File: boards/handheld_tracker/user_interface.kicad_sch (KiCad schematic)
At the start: 0 parts

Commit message: added test pads, UI buttons, and routed MCU pins
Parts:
- added SW1, SW10, SW11, SW12, SW13, SW14, SW15, SW2, SW3, SW4, SW5, SW6, SW7, SW8, SW9: SW_Push, Button_Switch_SMD:SW_SPST_PTS645, symbol Switch:SW_Push
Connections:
- new net +3.3V: SW1.1, SW10.1, SW11.1, SW12.1, SW13.1, SW14.1, SW15.1, SW2.1, SW3.1, SW4.1, SW5.1, SW6.1, SW7.1, SW8.1, SW9.1
- new net pushbutton_0: SW11.2
- new net pushbutton_1: SW1.2
- new net pushbutton_2: SW4.2
- new net pushbutton_3: SW7.2
- new net pushbutton_4: SW2.2
- new net pushbutton_5: SW5.2
- new net pushbutton_6: SW8.2
- new net pushbutton_7: SW3.2
- new net pushbutton_8: SW6.2
- new net pushbutton_9: SW9.2
- new net pushbutton_dot: SW10.2
- new net pushbutton_down: SW15.2
- new net pushbutton_enter: SW12.2
- new net pushbutton_menu: SW13.2
- new net pushbutton_up: SW14.2
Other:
- note added: "."
- note added: "0"
- note added: "1"
- note added: "2"
- note added: "3"
- note added: "4"
- note added: "5"
- note added: "6"
- note added: "7"
- note added: "8"
- note added: "9"
- note added: "<"
- note added: ">"
- note added: "ENTER"
- note added: "MENU"

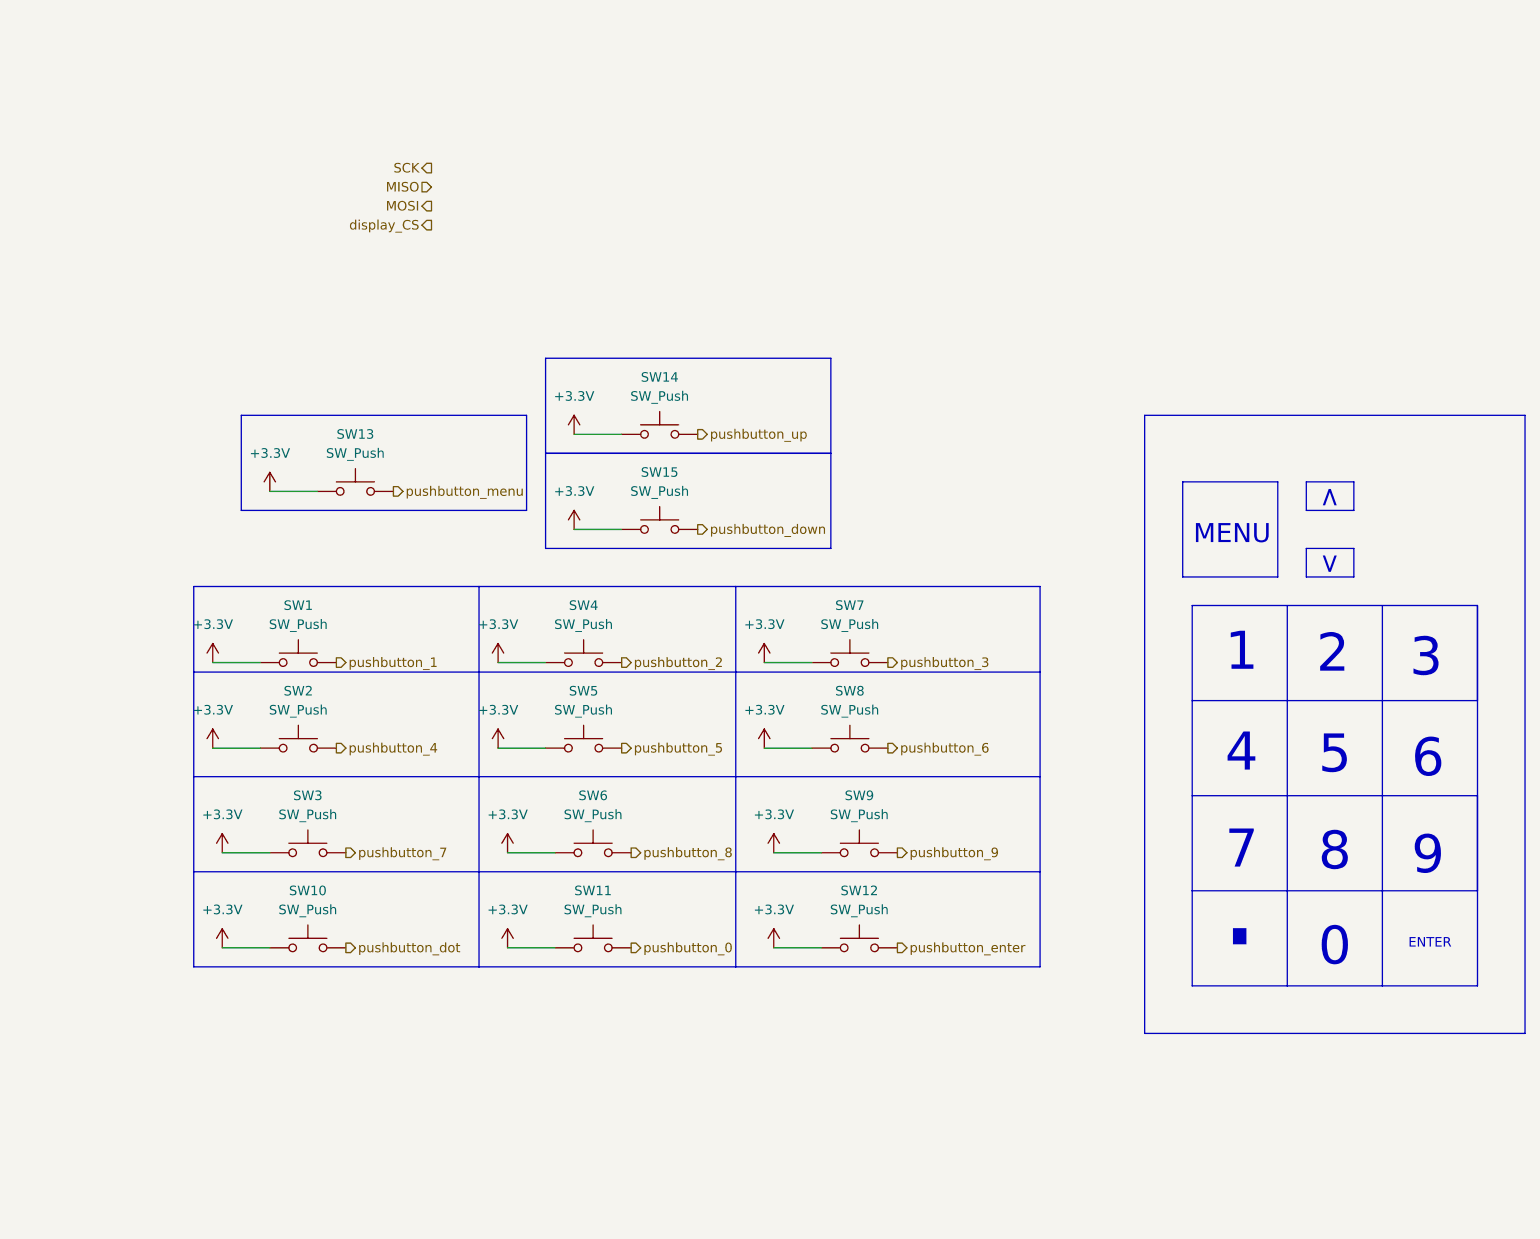
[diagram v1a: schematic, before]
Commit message: added all footprints and modified gitignore
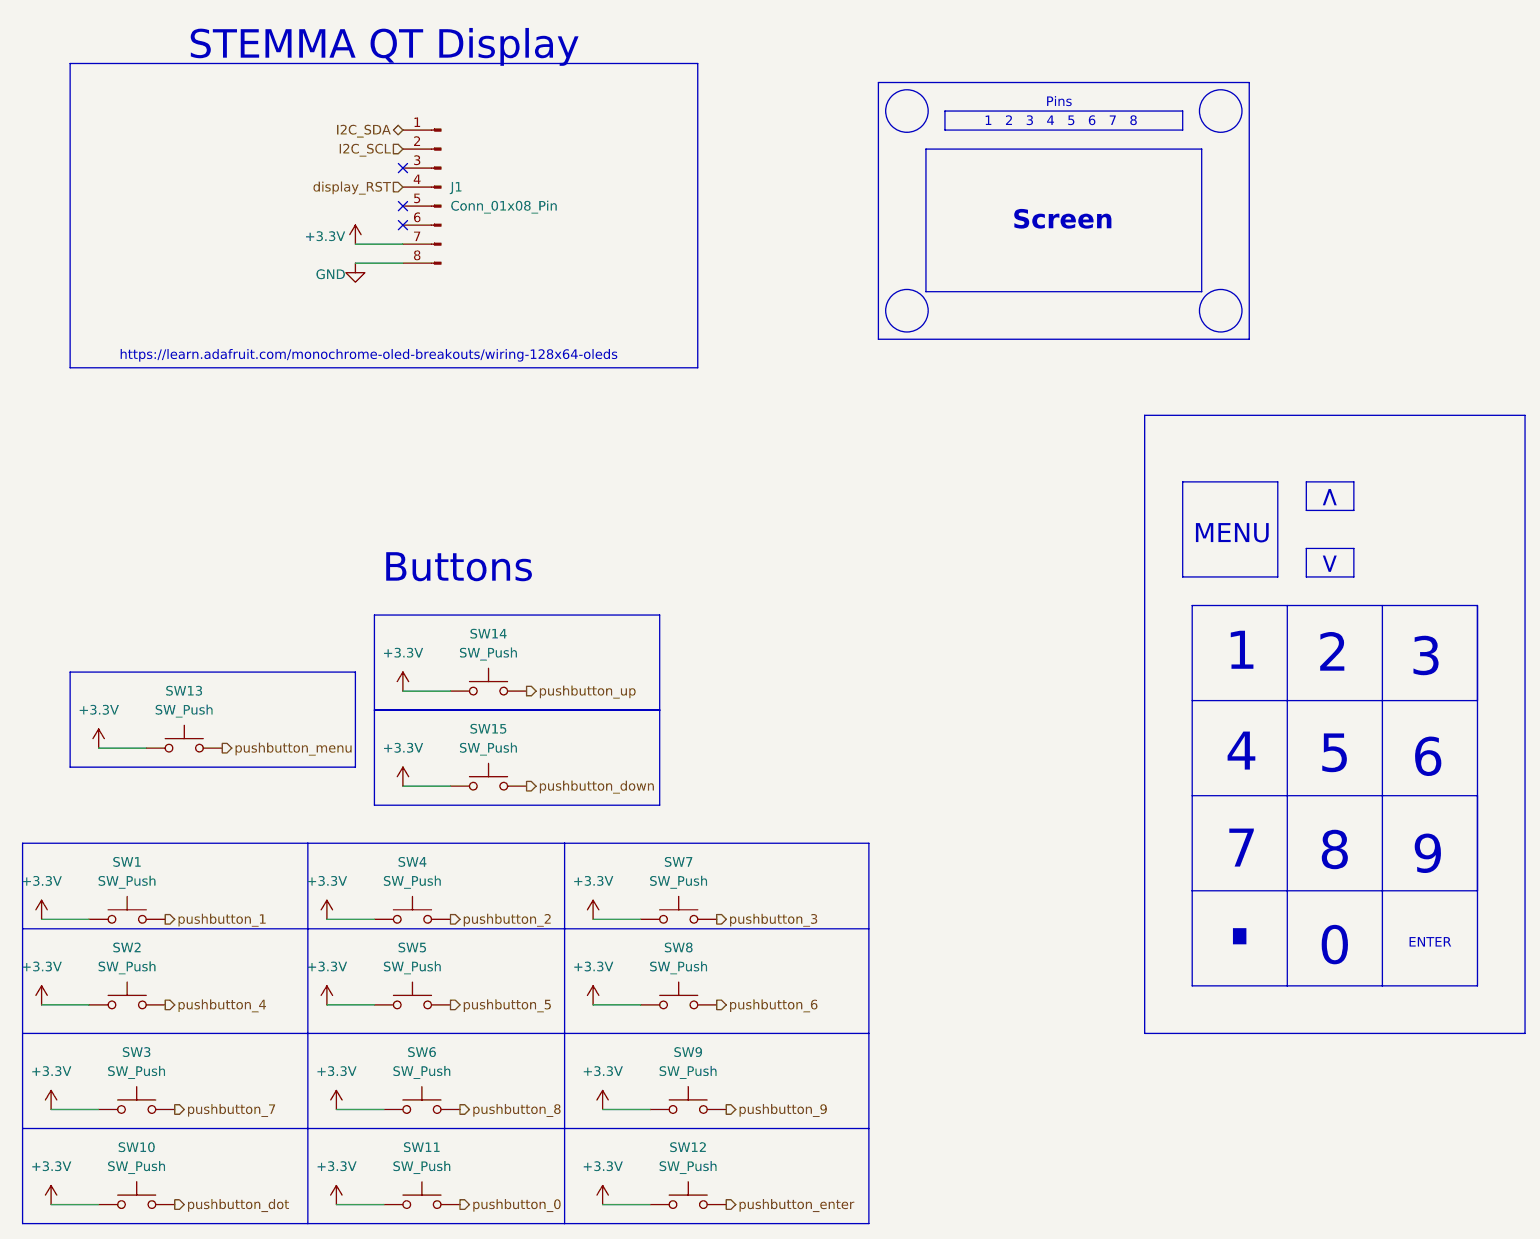
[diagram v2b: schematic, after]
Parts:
- added J1: Conn_01x08_Pin, Connector_PinSocket_2.54mm:PinSocket_1x08_P2.54mm_Vertical, symbol Connector:Conn_01x08_Pin
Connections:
- net +3.3V: now also J1.7 (Pin_7)
- new net GND: J1.8 (Pin_8)
- new net I2C_SCL: J1.2 (Pin_2)
- new net I2C_SDA: J1.1 (Pin_1)
- new net display_RST: J1.4 (Pin_4)
- no-connect marks 0 -> 3
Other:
- note added: "1 2 3 4 5 6 7 8"
- note added: "Buttons"
- note added: "Pins"
- note added: "STEMMA QT Display"
- note added: "Screen"
- note added: "https://learn.adafruit.com/monochrome-oled-breakouts/wiring-128x64-oleds"
- moved on the sheet: SW1, SW10, SW11, SW12, SW13, SW14, SW15, SW2, SW3, SW4, SW5, SW6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

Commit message: basic pcb layout
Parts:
- added H1: MountingHole, MountingHole:MountingHole_2.5mm_Pad, symbol Mechanical:MountingHole
- added H2, H3, H4: MountingHole, MountingHole:MountingHole_2.5mm_Pad_TopBottom, symbol Mechanical:MountingHole
- renumbered SW11 to SW0, SW4 to SW2, SW7 to SW3, SW2 to SW4, SW8 to SW6, SW3 to SW7, SW6 to SW8, SW10 to SW_DOT1, SW15 to SW_DOWN1, SW12 to SW_ENTER1, SW13 to SW_MENU1, SW14 to SW_UP1

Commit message: ignoring mounting holes for now
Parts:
- removed H1: MountingHole, MountingHole:MountingHole_2.5mm_Pad, symbol Mechanical:MountingHole
- removed H2, H3, H4: MountingHole, MountingHole:MountingHole_2.5mm_Pad_TopBottom, symbol Mechanical:MountingHole

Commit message: changed push buttons' 3v to ground, added conn component to power supply
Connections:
- net +3.3V: no longer SW0.1, SW1.1, SW2.1, SW3.1, SW4.1, SW5.1, SW6.1, SW7.1, SW8.1, SW9.1, SW_DOT1.1, SW_DOWN1.1, SW_ENTER1.1, SW_MENU1.1, SW_UP1.1
- net GND: now also SW0.1, SW1.1, SW2.1, SW3.1, SW4.1, SW5.1, SW6.1, SW7.1, SW8.1, SW9.1, SW_DOT1.1, SW_DOWN1.1, SW_ENTER1.1, SW_MENU1.1, SW_UP1.1
